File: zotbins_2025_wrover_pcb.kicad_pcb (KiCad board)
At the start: 2 copper layers, 80 x 82.5 mm, 26 parts, among them J1 FFC2B28-24-G, J2 Barrel Jack, J6 Conn_01x30_Pin, U2 MCP23017_SP, U3 XC6206P302MR-G, U4 XC6206P282PR-G, U5 LM7805_TO220, U6 ESP32-DEVKITC-32D

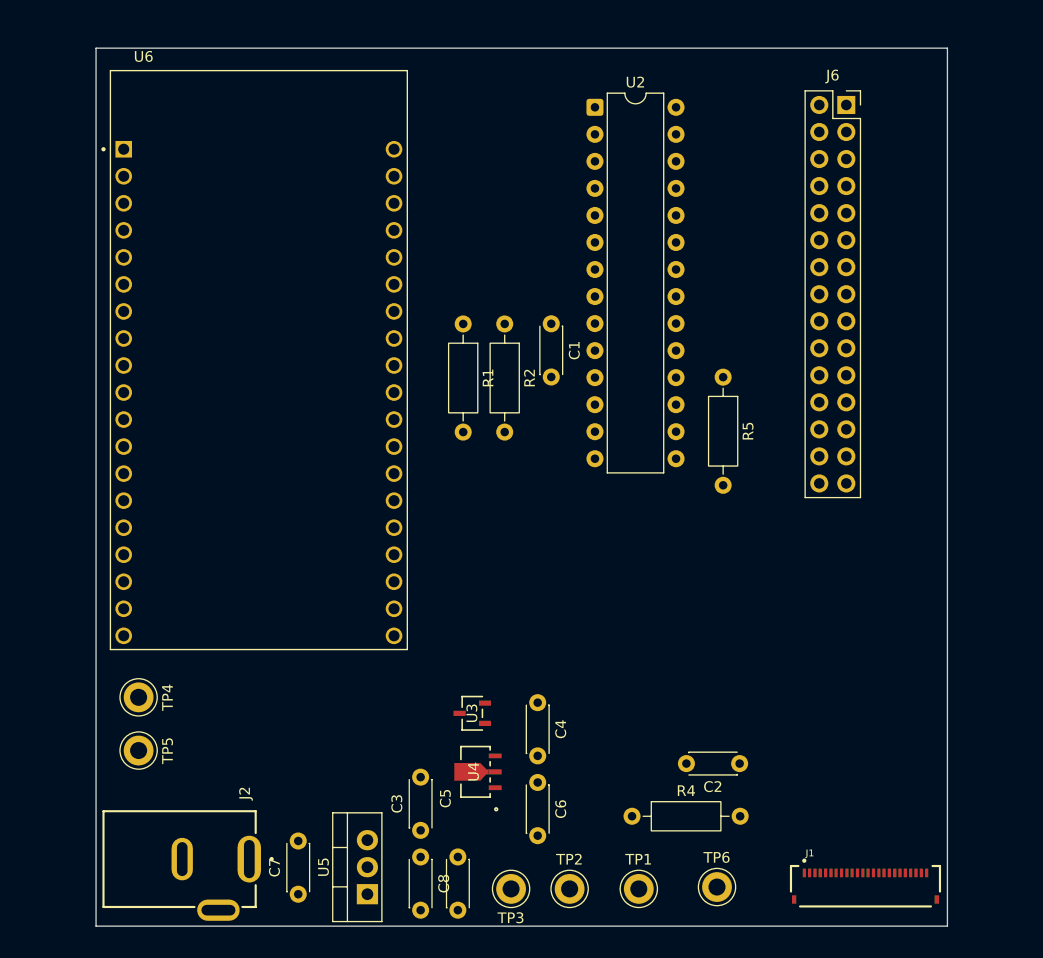
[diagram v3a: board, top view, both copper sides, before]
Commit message: completed power traces; currently ignoring DRC violations from ov2640 smd module ( 90+ violations :( )
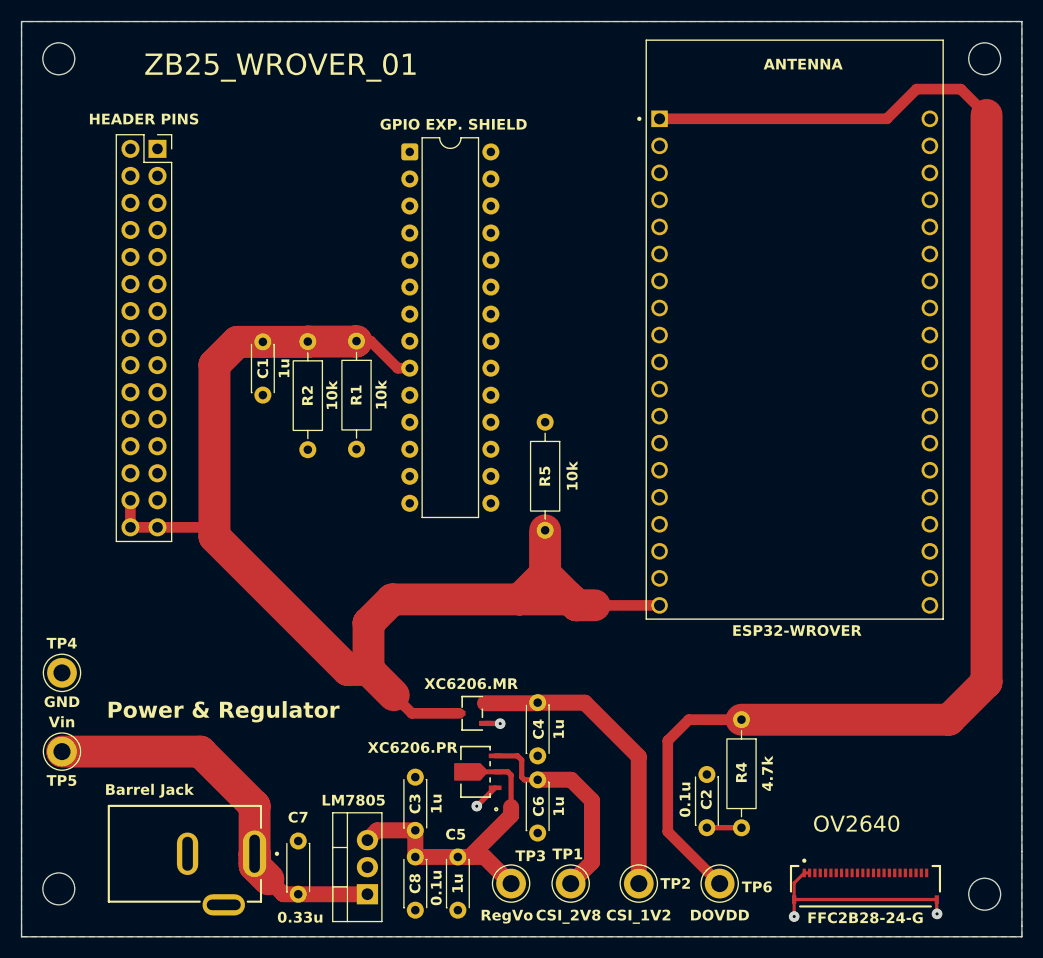
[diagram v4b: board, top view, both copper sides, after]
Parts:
- Barrel Jack: renamed from J2; value Barrel Jack -> J2
- GPIO EXP. SHIELD: renamed from U2
- HEADER PINS: renamed from J6
- moved HEADER PINS 64.9 mm to (105.8, 67.0)
- moved ESP32-WROVER 50.4 mm to (165.7, 83.9)
- moved C1 27.2 mm to (115.7, 85.1)
- moved R2 18.6 mm to (119.9, 85.1)
- moved GPIO EXP. SHIELD 17.9 mm to (129.5, 67.2)
- moved R5 17.3 mm to (142.2, 92.6)
- moved R4 13.7 mm to (160.7, 120.6), turned to -90 degrees
- moved R1 10.2 mm to (124.5, 85.0)
- moved TP4 7.56 mm to (96.8, 116.2), turned to 0 degrees
- moved TP5 7.20 mm to (96.8, 123.6), turned to 180 degrees
- moved C2 6.76 mm to (157.4, 130.8), turned to 90 degrees
- moved TP2 6.52 mm to (151.0, 136.0)
- moved TP1 6.42 mm to (144.6, 136.0)
- moved Barrel Jack 0.71 mm to (108.3, 133.2)
- moved C3 0.50 mm to (130.0, 131.0)
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- renumbered U6 to ESP32-WROVER, J1 to FFC2B28-24-G, U5 to LM7805, U3 to XC6206.MR, U4 to XC6206.PR
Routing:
- net +5V: track 0.00 -> 151.2 mm
- net +3V3: track 0.00 -> 133.9 mm
- net Net-(U5-VI): track 0.00 -> 38.4 mm
- net CSI_1V2: track 0.00 -> 28.5 mm
- net GND: track 0.00 -> 23.5 mm, vias 0 -> 4
- net CSI_2V8: track 0.00 -> 20.4 mm
- net /RESETB: track 0.00 -> 3.25 mm
- added copper zone on B.Cu, net GND
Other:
- board size 80 x 82.5 mm -> 94 x 86 mm
- board text added: "ANTENNA"
- board text added: "OV2640"
- board text added: "Power & Regulator"
- board text added: "ZB25_WROVER_01"

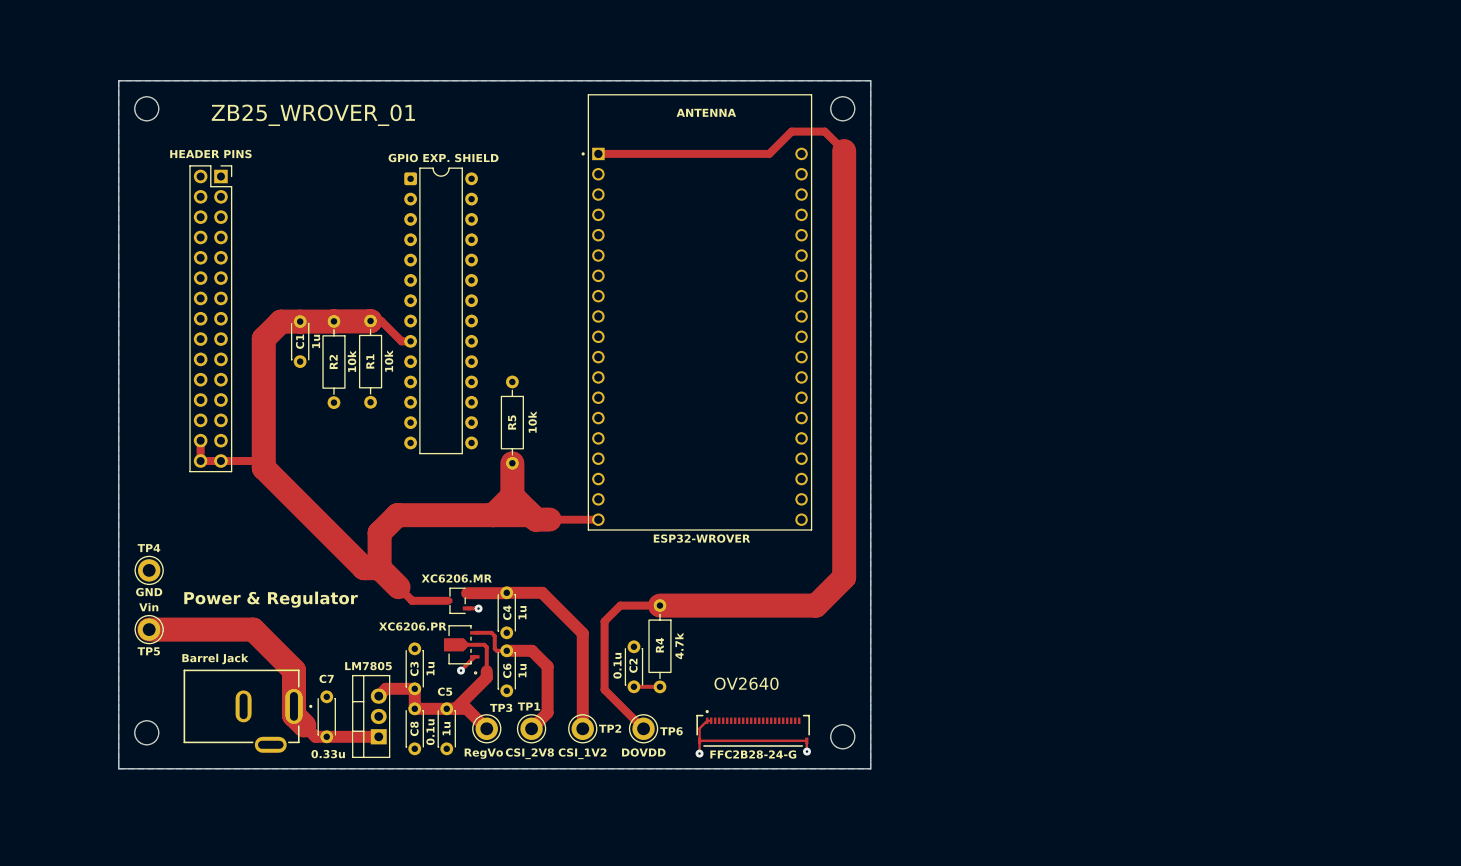
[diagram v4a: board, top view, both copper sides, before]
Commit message: partially completed gpio shield
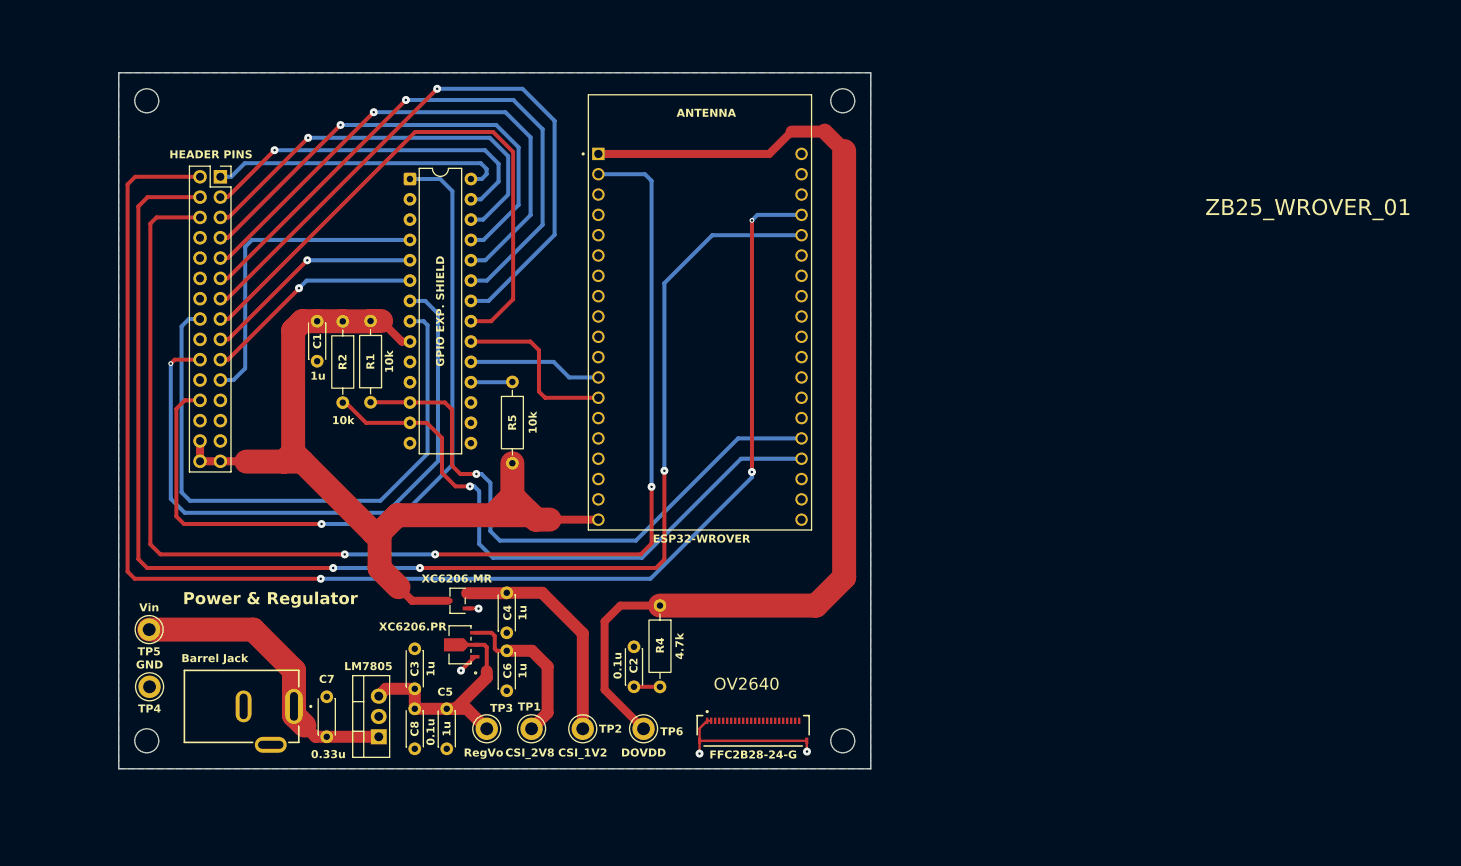
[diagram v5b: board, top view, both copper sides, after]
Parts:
- moved TP4 14.6 mm to (96.8, 130.8), turned to 180 degrees
- moved C1 2.13 mm to (117.8, 85.0)
- moved R2 1.10 mm to (121.0, 85.1)
- moved GPIO EXP. SHIELD 0.08 mm to (129.4, 67.3)
- moved HEADER PINS 0.08 mm to (105.7, 67.0)
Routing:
- net /TX: track 0.00 -> 180.1 mm, vias 0 -> 3
- net /RX: track 0.00 -> 173.1 mm, vias 0 -> 3
- net /EN: track 0.00 -> 162.7 mm, vias 0 -> 3
- net /TRIG: track 0.00 -> 95.0 mm, vias 0 -> 1
- net /GPA1: track 0.00 -> 82.4 mm, vias 0 -> 1
- net /GPB6: track 0.00 -> 80.2 mm, vias 0 -> 1
- net /GPIO_SCK: track 0.00 -> 76.6 mm, vias 0 -> 1
- net /IR: track 0.00 -> 75.5 mm
- net /GPA2: track 0.00 -> 74.8 mm, vias 0 -> 1
- net /GPIO_SDA: track 0.00 -> 74.0 mm, vias 0 -> 1
- net /GPA0: track 0.00 -> 72.1 mm
- net /GPA3: track 0.00 -> 67.1 mm, vias 0 -> 1
- net /GPA4: track 0.00 -> 59.2 mm, vias 0 -> 1
- net /GPA5: track 0.00 -> 51.8 mm, vias 0 -> 1
- net /GPA6: track 0.00 -> 44.5 mm, vias 0 -> 1
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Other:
- board size 94 x 86 mm -> 94 x 87 mm

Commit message: camera module connections left -- need to make constraints more marginal to account for tight smd constraints. (65 drc violations from footprint alone)
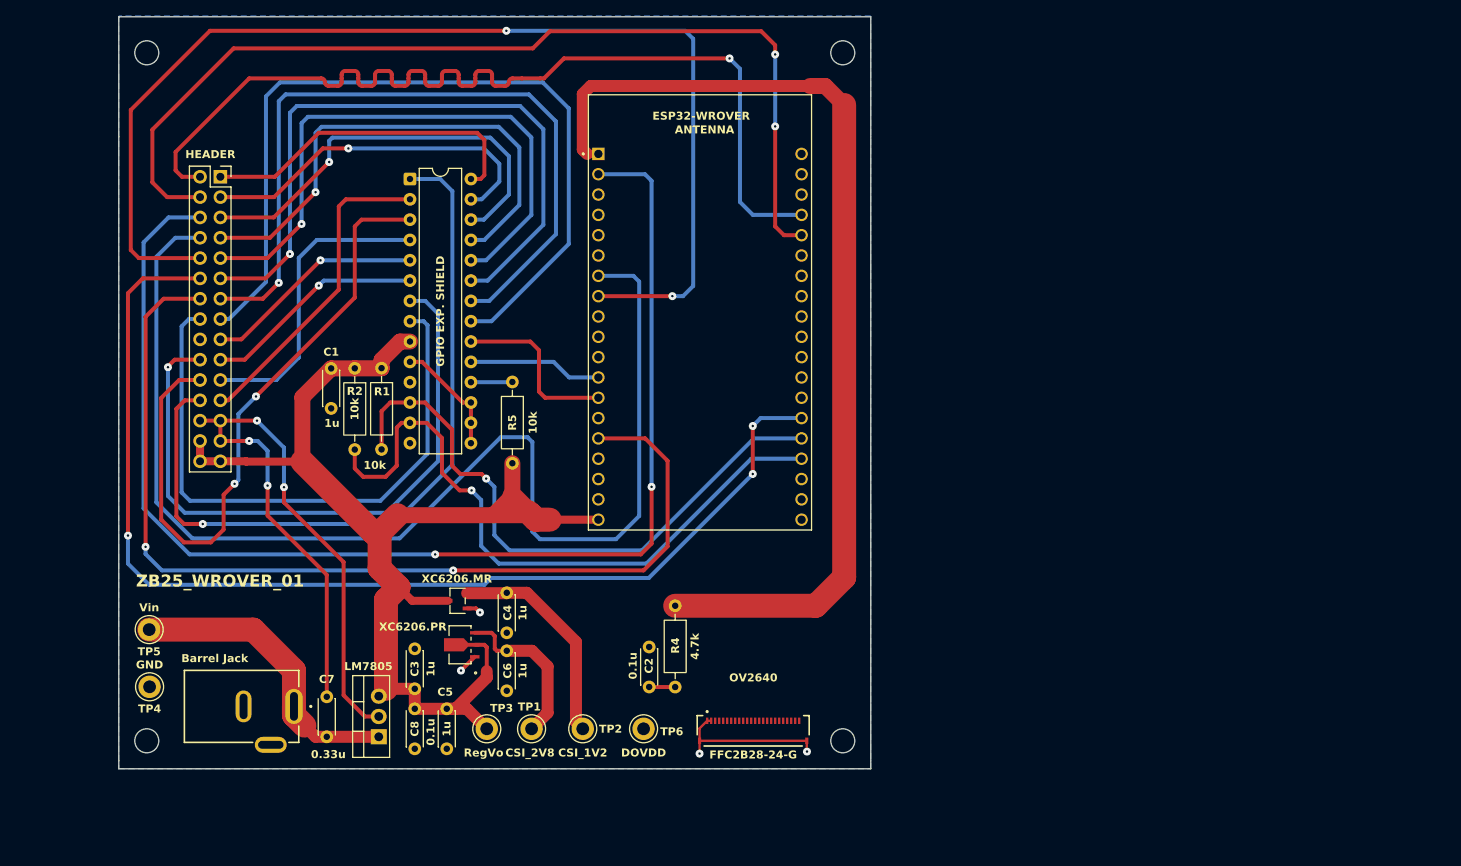
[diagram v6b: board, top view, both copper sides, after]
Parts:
- HEADER: renamed from HEADER PINS
- moved C1 6.15 mm to (119.5, 91.0)
- moved R2 6.06 mm to (122.5, 90.9)
- moved R1 6.05 mm to (125.8, 90.9)
- moved C2 1.90 mm to (159.3, 130.8)
- moved R4 1.90 mm to (162.6, 120.6)
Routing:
- net /GPIO32: track 0.00 -> 152.3 mm
- net /GPIO33: track 0.00 -> 144.7 mm, vias 0 -> 2
- net /GPIO0: track 0.00 -> 141.0 mm, vias 0 -> 3
- net /GPIO13: track 0.00 -> 125.2 mm, vias 0 -> 2
- net GND: track 23.5 -> 132.9 mm, vias 4 -> 8
- net /SCK: track 0.00 -> 82.6 mm, vias 0 -> 2
- net /TX: track 180.1 -> 121.9 mm, vias 3 -> 1
- net /RX: track 173.1 -> 123.4 mm, vias 3 -> 2
- net /ECHO: track 0.00 -> 40.2 mm
- net /GPA0: track 72.1 -> 103.9 mm
- net /GPA1: track 82.4 -> 95.3 mm
- net /GPA2: track 74.8 -> 84.6 mm
- net +3V3: track 133.9 -> 124.9 mm
- net /GPA3: track 67.1 -> 74.1 mm
- net /GPIO_SCK: track 76.6 -> 82.8 mm
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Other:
- board size 94 x 87 mm -> 94 x 94 mm
- board text removed: "Power & Regulator"

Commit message: current traces finished; todo: add servo + other peripheral terminal screws + adjust pcb size
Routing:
- net /XCLK1: track 0.00 -> 96.9 mm, vias 0 -> 1
- net /DATA4: track 0.00 -> 93.5 mm, vias 0 -> 2
- net /DATA5: track 0.00 -> 88.4 mm, vias 0 -> 2
- net /HREF: track 0.00 -> 84.1 mm, vias 0 -> 2
- net /DATA6: track 0.00 -> 81.4 mm, vias 0 -> 2
- net /DATA3: track 0.00 -> 80.9 mm, vias 0 -> 1
- net /DATA2: track 0.00 -> 79.3 mm, vias 0 -> 1
- net /PCLK: track 0.00 -> 79.1 mm, vias 0 -> 2
- net /DATA7: track 0.00 -> 73.3 mm, vias 0 -> 2
- net /DATA1: track 0.00 -> 67.6 mm, vias 0 -> 1
- net /VSYNC: track 0.00 -> 67.2 mm, vias 0 -> 2
- net /SIOD: track 0.00 -> 63.8 mm, vias 0 -> 2
- net /SIOC: track 0.00 -> 58.2 mm, vias 0 -> 2
- net +3V3: track 124.9 -> 176.4 mm, vias 0 -> 1
- net /DATA0: track 0.00 -> 50.1 mm, vias 0 -> 1
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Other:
- board size 94 x 94 mm -> 107 x 104 mm
- board text added: "ZB25_WROVER-DEV_01"
- board text removed: "ZB25_WROVER_01"

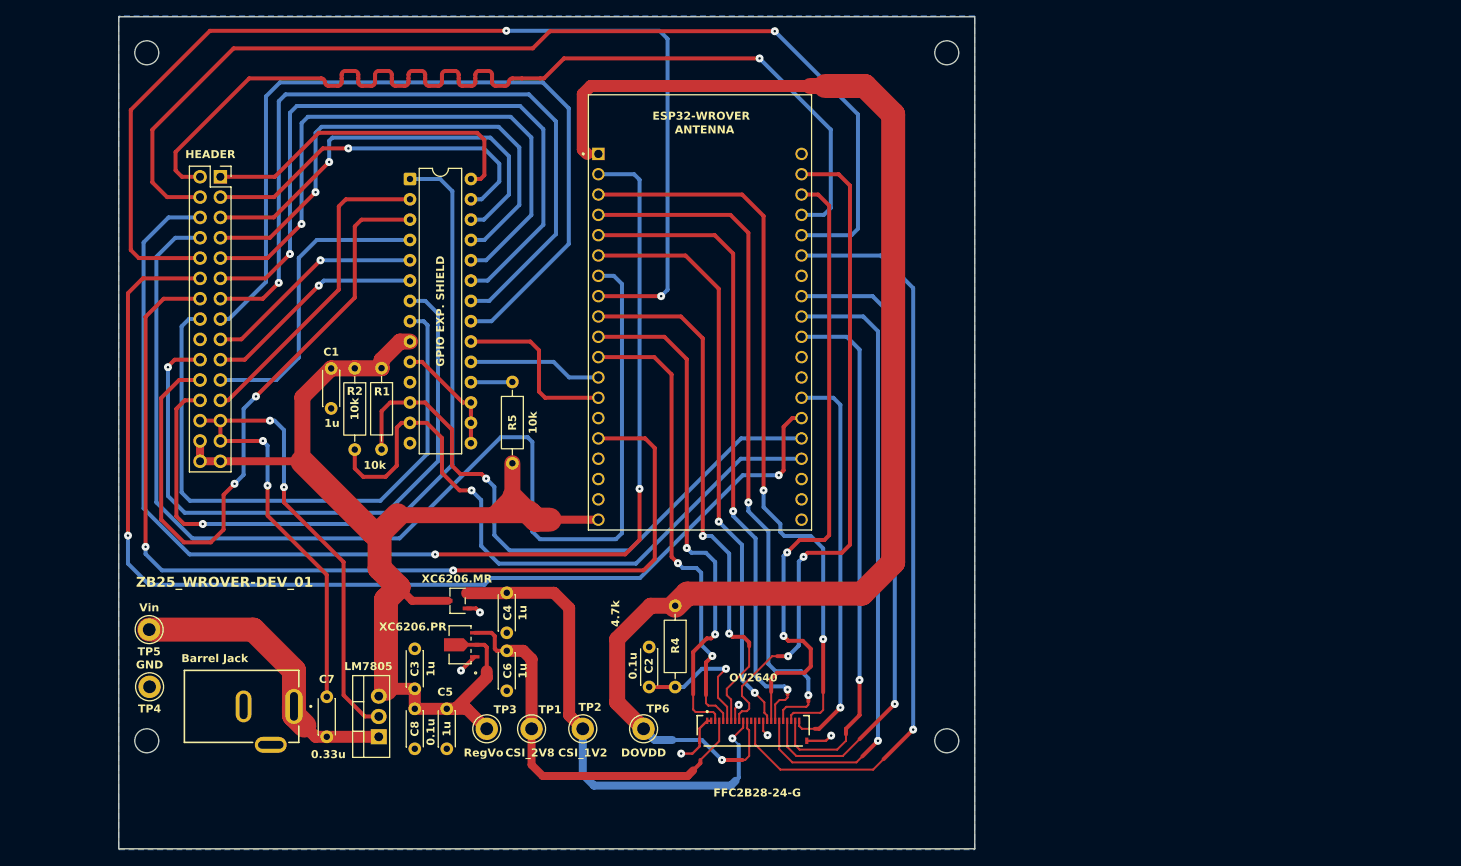
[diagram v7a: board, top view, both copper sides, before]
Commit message: minor adjustments and size adjustment. Ready for final stage -- ALL PERIPHERALS. The current version is the most minimal version of a devboard.
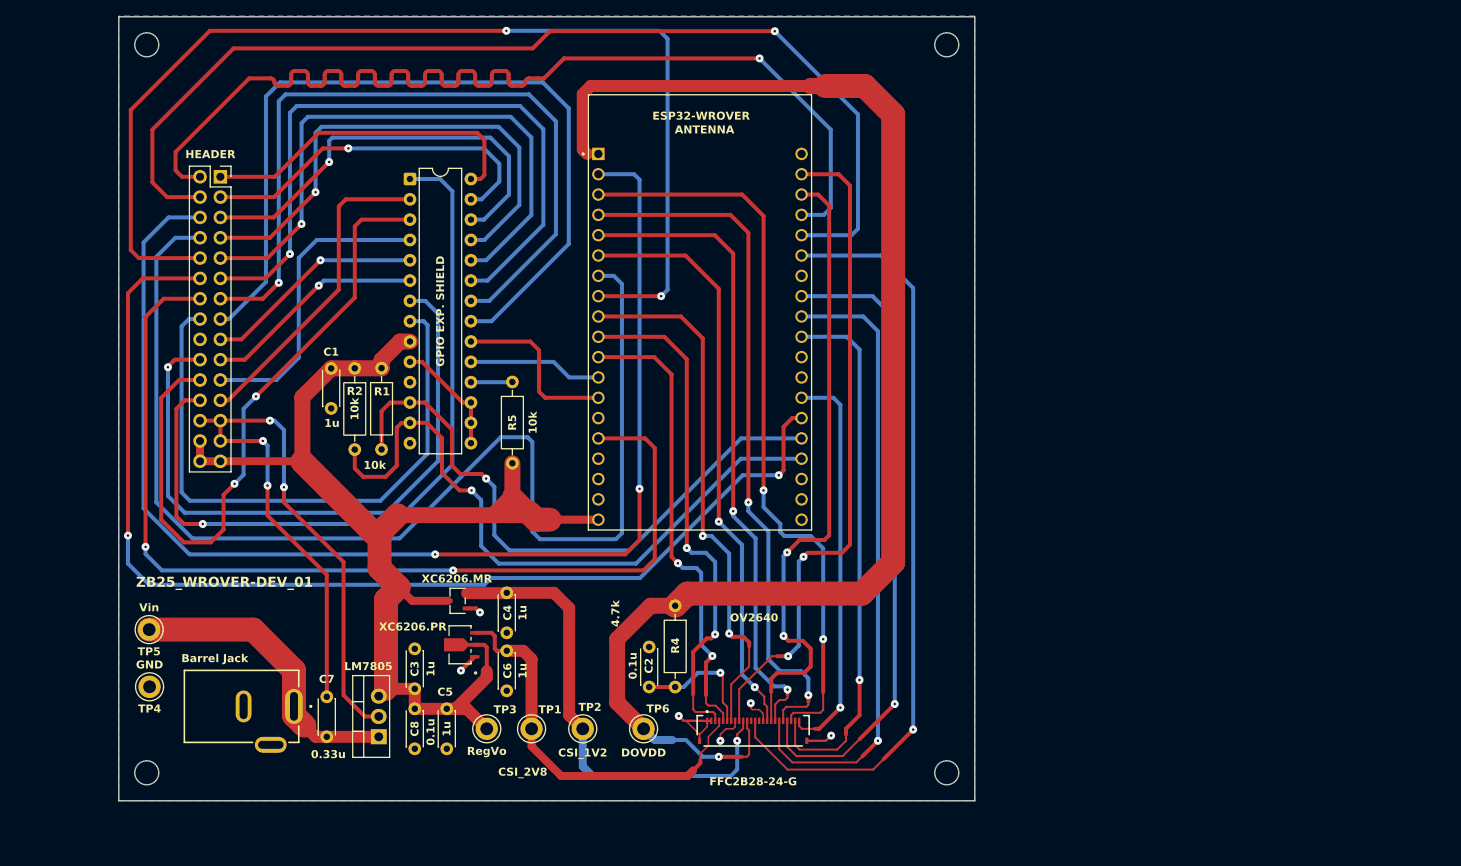
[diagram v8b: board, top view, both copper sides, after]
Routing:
- net GND: track 129.1 -> 135.2 mm
- net /TX: track 125.2 -> 130.8 mm
- net CSI_1V2: track 63.6 -> 60.6 mm
- net /RESETB: track 17.9 -> 16.0 mm
- net CSI_2V8: track 51.2 -> 49.9 mm
- net /HREF: track 84.1 -> 83.0 mm
- net /DATA6: track 81.4 -> 80.8 mm
- net /XCLK1: track 96.9 -> 96.4 mm
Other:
- board size 107 x 104 mm -> 107 x 98 mm
